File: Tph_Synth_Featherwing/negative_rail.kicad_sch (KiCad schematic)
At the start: 5 parts, among them U2 LM2663M

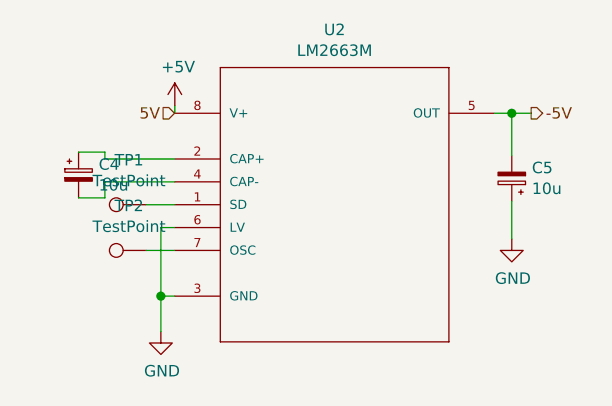
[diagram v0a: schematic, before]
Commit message: Upgrade design to KiCad 10; clear ERC and DRC violations
Co-authored-by: Copilot <223556219+Copilot@users.noreply.github.com>
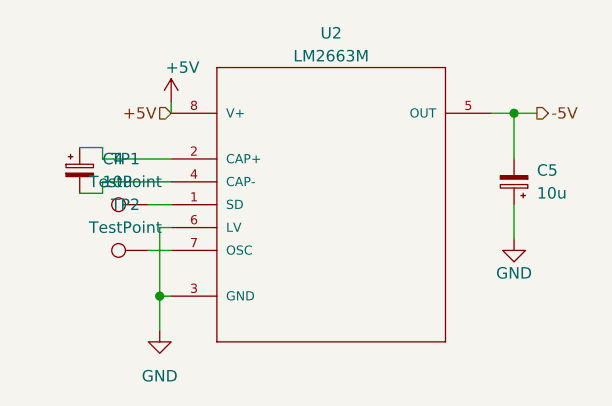
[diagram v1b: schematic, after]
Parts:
- C4, C5: symbol Device:CP_Small -> Device:C_Polarized_Small
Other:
- moved on the sheet: C4

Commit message: Release v0.4 with complete KiCad 10 schematic-PCB parity
Synchronize pad nets, schematic paths, component fields and BOM exclusions while retaining routing and placement. Restore project-local STEP models, fix edge silkscreen using local footprint variants, update revision metadata and improve schematic readability. Include inspected PDF and PCB renders.

Co-authored-by: Copilot <223556219+Copilot@users.noreply.github.com>
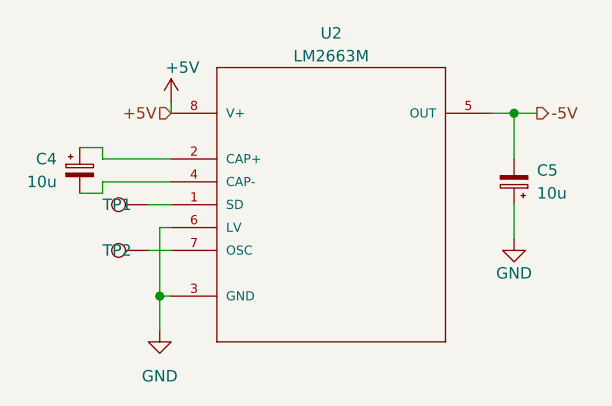
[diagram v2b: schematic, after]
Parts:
- TP1, TP2: now left out of the parts list
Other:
- title: (none) -> 3-Phase Synth FeatherWing
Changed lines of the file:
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@@
 	(generator_version "10.0")
 	(paper "A4")
+	(title_block
+		(title "3-Phase Synth FeatherWing")
+		(date "2026-10-28")
+		(rev "0.4")
+	)
 	(junction
 		(at 120.65 95.25)
@@
 		(dnp no)
 		(property "Reference" "C4"
-			(at 114.3 80.01 0)
-			(show_name no)
-			(do_not_autoplace no)
-			(effects
-				(font
-					(size 1.27 1.27)
-				)
-				(justify left)
+			(at 109.22 80.01 0)
+			(show_name no)
+			(do_not_autoplace no)
+			(effects
+				(font
+					(size 1.27 1.27)
+				)
+				(justify right)
 			)
 		)
 		(property "Value" "10u"
-			(at 114.3 82.55 0)
-			(show_name no)
-			(do_not_autoplace no)
-			(effects
-				(font
-					(size 1.27 1.27)
-				)
-				(justify left)
+			(at 109.22 82.55 0)
+			(show_name no)
+			(do_not_autoplace no)
+			(effects
+				(font
+					(size 1.27 1.27)
+				)
+				(justify right)
 			)
 		)
@@
 		(body_style 1)
 		(exclude_from_sim no)
-		(in_bom yes)
+		(in_bom no)
 		(on_board yes)
 		(in_pos_files yes)
 		(dnp no)
 		(property "Reference" "TP2"
-			(at 116.84 85.09 90)
-			(show_name no)
-			(do_not_autoplace no)
-			(effects
-				(font
-					(size 1.27 1.27)
-				)
+			(at 114.3 90.17 90)
+			(show_name no)
+			(do_not_autoplace no)
+			(effects
+				(font
+					(size 1.27 1.27)
+				)
+				(justify right)
 			)
 		)
@@
 					(size 1.27 1.27)
 				)
-			)
+				(justify right)
+			)
+			(hide yes)
 		)
 		(property "Footprint" "TestPoint:TestPoint_Pad_D1.0mm"
@@
 		(body_style 1)
 		(exclude_from_sim no)
-		(in_bom yes)
+		(in_bom no)
 		(on_board yes)
 		(in_pos_files yes)
 		(dnp no)
 		(property "Reference" "TP1"
-			(at 116.84 80.01 90)
-			(show_name no)
-			(do_not_autoplace no)
-			(effects
-				(font
-					(size 1.27 1.27)
-				)
+			(at 114.3 85.09 90)
+			(show_name no)
+			(do_not_autoplace no)
+			(effects
+				(font
+					(size 1.27 1.27)
+				)
+				(justify right)
 			)
 		)
@@
 					(size 1.27 1.27)
 				)
-			)
+				(justify right)
+			)
+			(hide yes)
 		)
 		(property "Footprint" "TestPoint:TestPoint_Pad_D1.0mm"
